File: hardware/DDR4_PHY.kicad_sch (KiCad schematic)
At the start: 2 parts, among them U1 RK3562, U2 FJBD4N8GT6L9-SKC

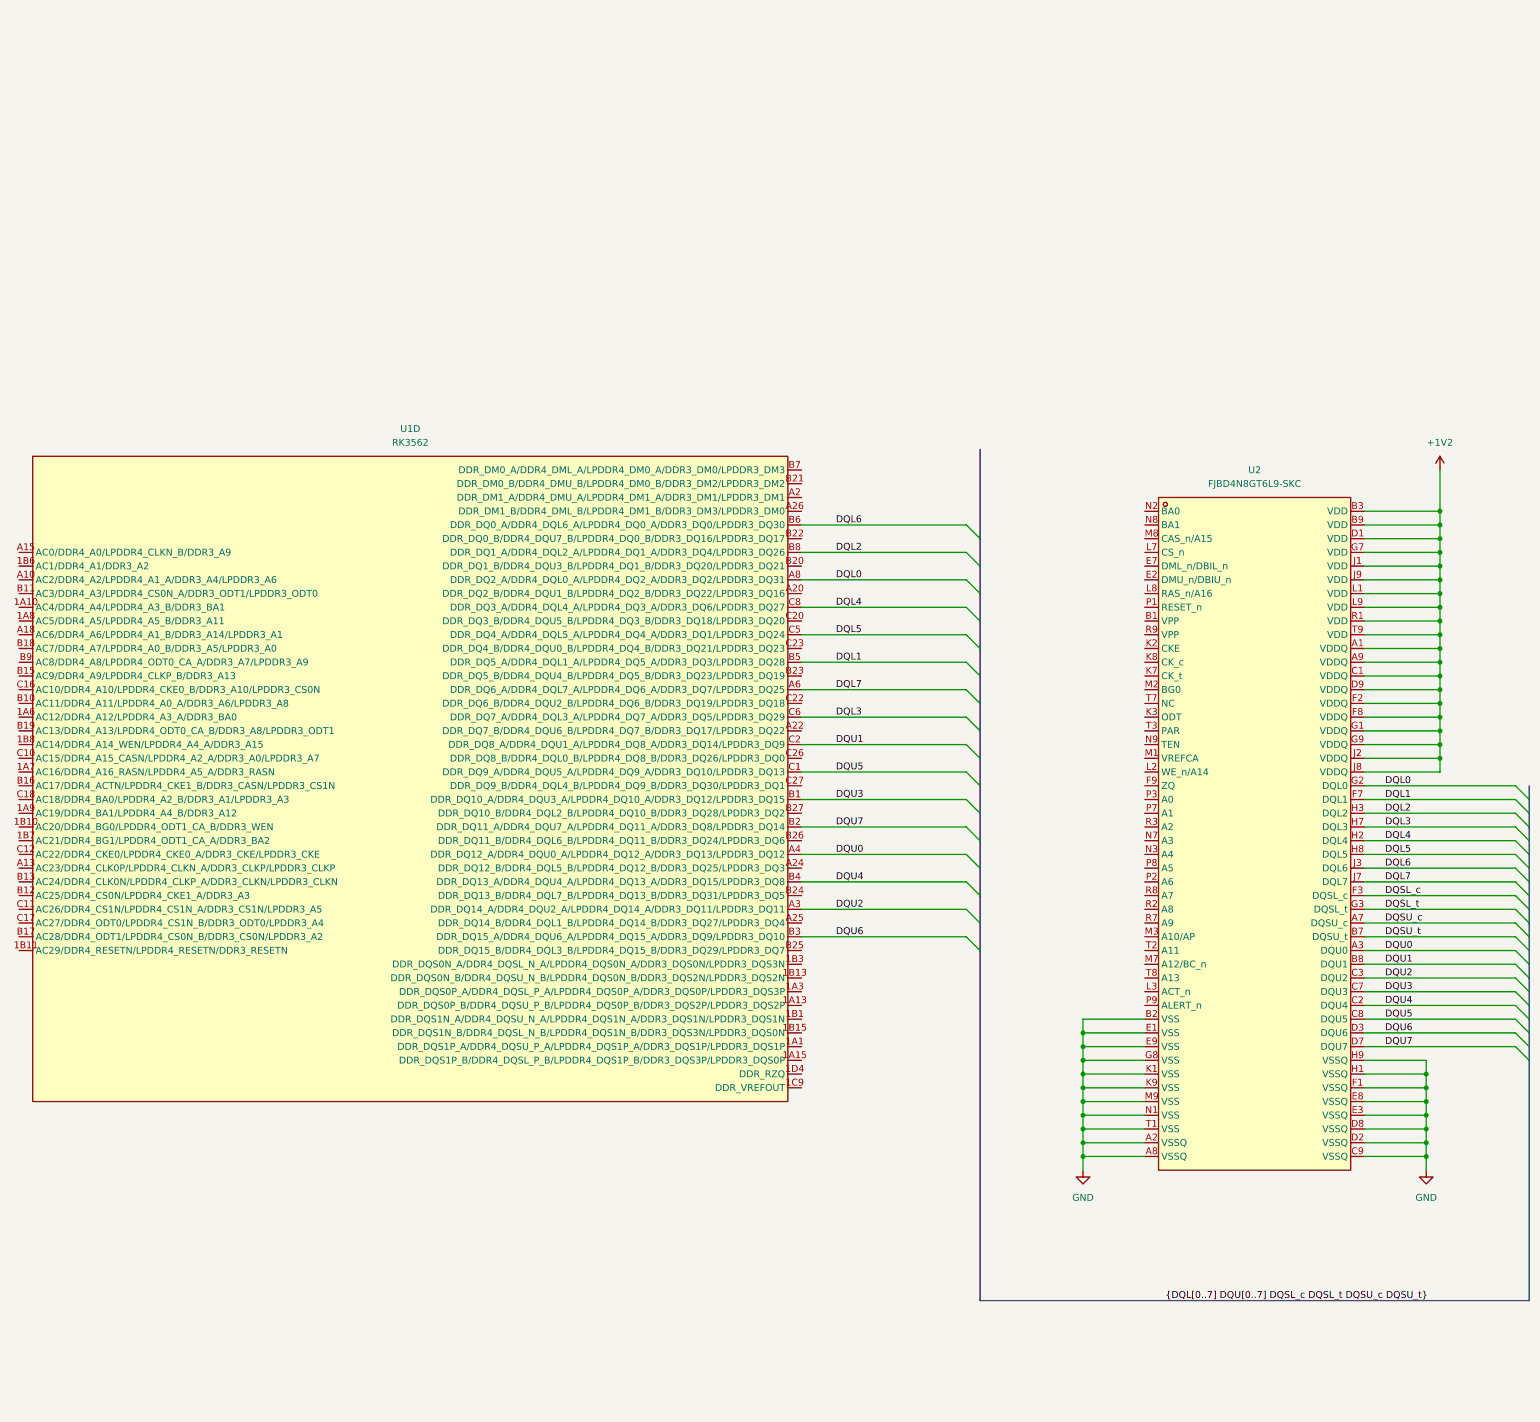
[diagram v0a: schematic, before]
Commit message: DDR4 schematic almost completed
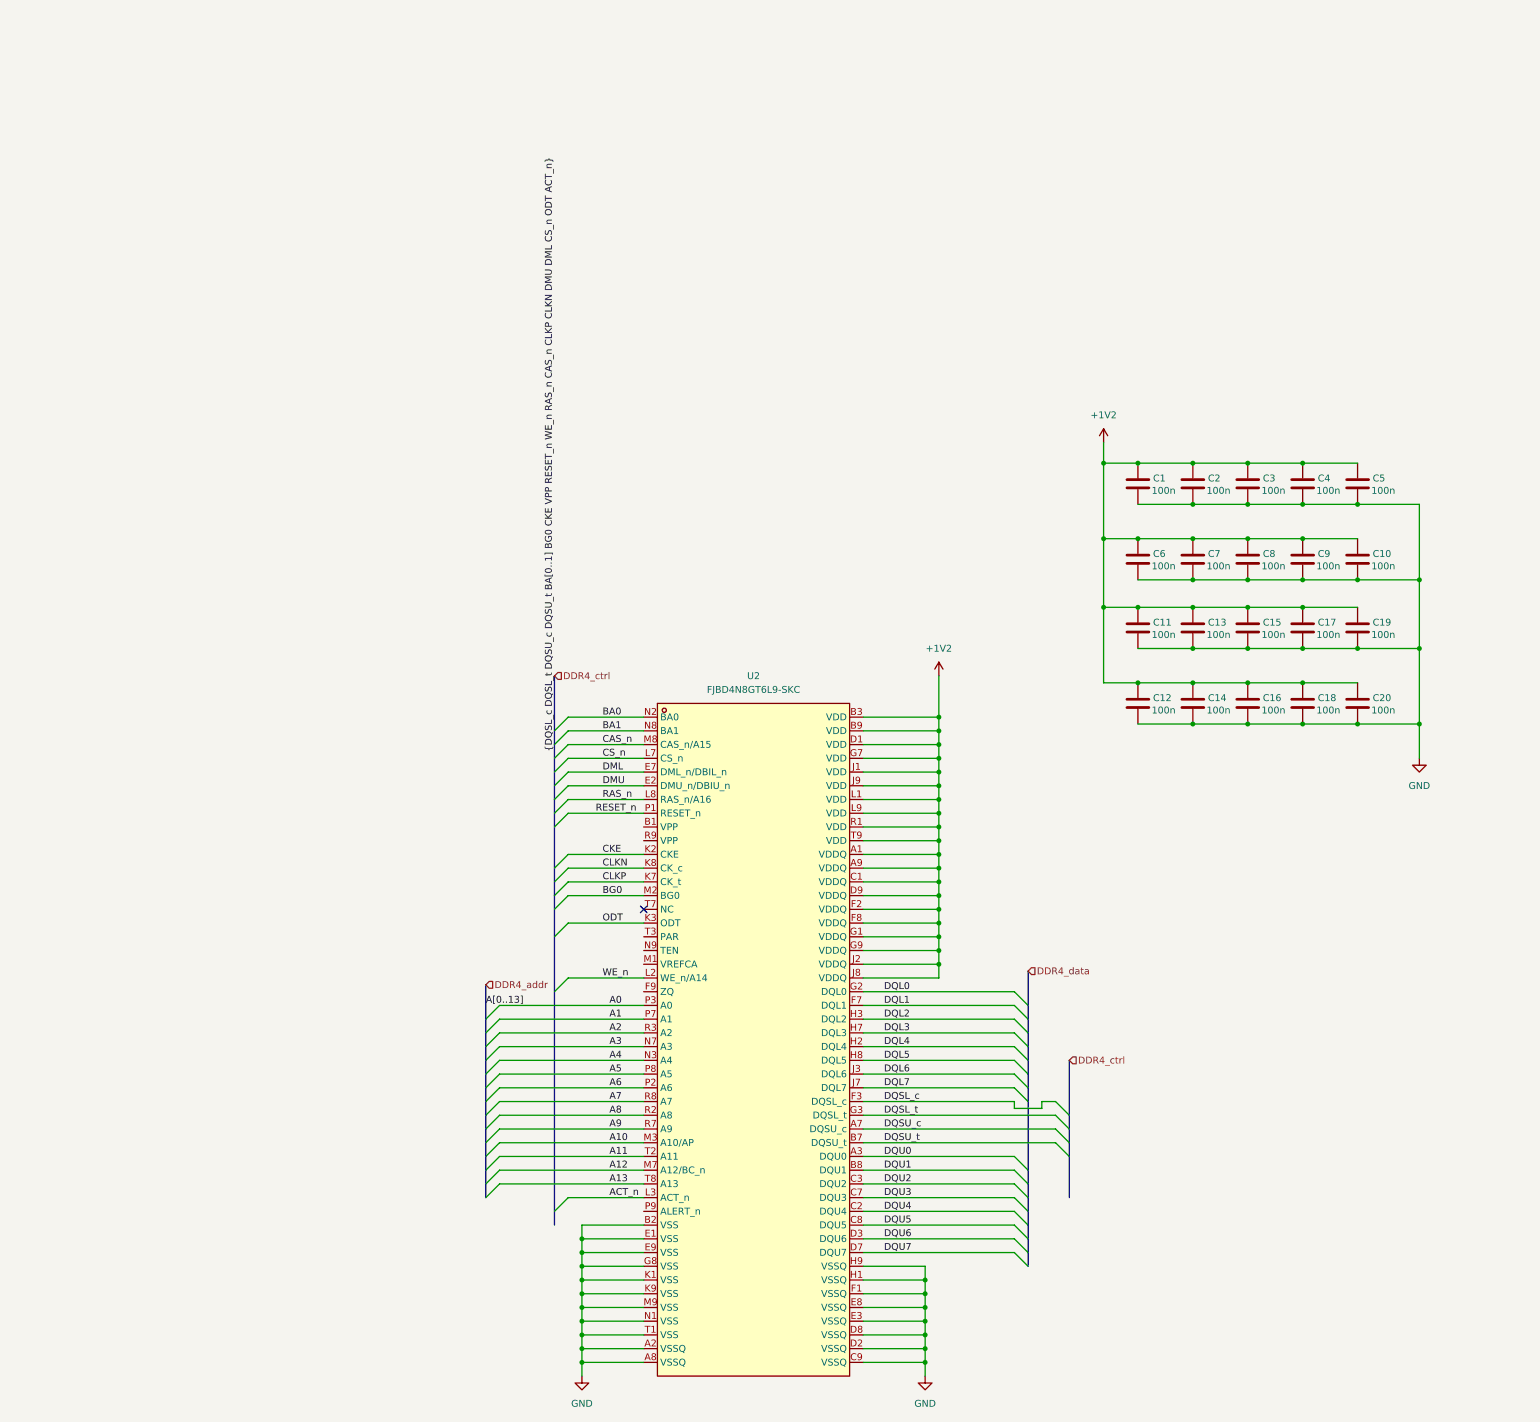
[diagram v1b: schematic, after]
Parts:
- removed U1: RK3562, Package_BGA:RK3562, symbol easyeda2kicad:RK3562
- added C1, C10, C11, C12, C13, C14, C15, C16, C17, C18, C19, C2, C20, C3, C4, C5, C6, C7, C8, C9: 100n, Capacitor_SMD:C_0201_0603Metric, symbol Device:C
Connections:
- net +1V2: now also C1.1, C10.1, C11.1, C12.1, C13.1, C14.1, C15.1, C16.1, C17.1, C18.1, C19.1, C2.1, C20.1, C3.1, C4.1, C5.1, C6.1, C7.1, C8.1, C9.1
- net GND: now also C1.2, C10.2, C11.2, C12.2, C13.2, C14.2, C15.2, C16.2, C17.2, C18.2, C19.2, C2.2, C20.2, C3.2, C4.2, C5.2, C6.2, C7.2, C8.2, C9.2
- net DMU: now reaches U2.E2 (DMU_n/DBIU_n)
- net DML: now reaches U2.E7 (DML_n/DBIL_n)
- net CKE: now reaches U2.K2 (CKE)
- net ODT: now reaches U2.K3 (ODT)
- net CLKP: now reaches U2.K7 (CK_t)
- net CLKN: now reaches U2.K8 (CK_c)
- net WE_n: now reaches U2.L2 (WE_n/A14)
- net ACT_n: now reaches U2.L3 (ACT_n)
- net CS_n: now reaches U2.L7 (CS_n)
- net RAS_n: now reaches U2.L8 (RAS_n/A16)
- net BG0: now reaches U2.M2 (BG0)
- net A10: now reaches U2.M3 (A10/AP)
- net A12: now reaches U2.M7 (A12/BC_n)
- net CAS_n: now reaches U2.M8 (CAS_n/A15)
- net BA0: now reaches U2.N2 (BA0)
- net A4: now reaches U2.N3 (A4)
- net A3: now reaches U2.N7 (A3)
- net BA1: now reaches U2.N8 (BA1)
- net RESET_n: now reaches U2.P1 (RESET_n)
- net A6: now reaches U2.P2 (A6)
- net A0: now reaches U2.P3 (A0)
- net A1: now reaches U2.P7 (A1)
- net A5: now reaches U2.P8 (A5)
- net A8: now reaches U2.R2 (A8)
- net A2: now reaches U2.R3 (A2)
- net A9: now reaches U2.R7 (A9)
- net A7: now reaches U2.R8 (A7)
- net A11: now reaches U2.T2 (A11)
- net A13: now reaches U2.T8 (A13)
- no-connect marks 0 -> 1
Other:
- moved on the sheet: U2
